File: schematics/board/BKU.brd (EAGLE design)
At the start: 94 x 94 mm, 66 parts, among them Q1 8MHz, Q2 32,768KHz, U1 STM32F405RGT6

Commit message: Добавлена батарейка в БКУ
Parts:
- added BT1: 6.8MM_COIN_CELL, SparkFun-Batteries:BATTCON-6.8MM
- added D1: BB141, diode:SOD523
- added R4: 620R, resistor:R0603
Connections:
- removed net VBAT: U1.1
- new net N$1: BT1.+, R4.1
- new net N$2: D1.C, R4.2, U1.1
- net GND: now also BT1.-
- net VDD: now also D1.A

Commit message: Изменения в БКУ
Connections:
- net 5V: now also RADIO.P$6
- net VDD: no longer RADIO.P$6
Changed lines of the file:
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@@
 <wire x1="0" y1="59.5" x2="0" y2="34.5" width="0.1524" layer="20"/>
 <wire x1="0" y1="23" x2="0" y2="25.5" width="0.1524" layer="20"/>
-<hole x="46.5" y="30" drill="6.5"/>
-<circle x="46.5" y="30" radius="4.5" width="0.1524" layer="21"/>
+<hole x="46" y="30" drill="6.5"/>
+<circle x="46" y="30" radius="4.5" width="0.1524" layer="21"/>
 <rectangle x1="39.972" y1="40.038" x2="51.972" y2="57.038" layer="29" rot="R180"/>
 <rectangle x1="39.97" y1="40.04" x2="51.97" y2="57.04" layer="41"/>
@@
 <wire x1="65.61" y1="32.57" x2="65.33" y2="32.85" width="0.25" layer="1"/>
 <wire x1="65.33" y1="32.85" x2="63.84" y2="32.85" width="0.25" layer="1"/>
+<contactref element="RADIO" pad="P$6"/>
+<wire x1="53.5" y1="76.55" x2="60.97" y2="86.6" width="0" layer="19" extent="1-1"/>
 <wire x1="83.73" y1="64.6" x2="60.97" y2="86.6" width="0" layer="19" extent="1-1"/>
 <wire x1="86.6" y1="53.35" x2="83.73" y2="64.6" width="0" layer="19" extent="1-1"/>
@@
 <contactref element="U$20" pad="10"/>
 <contactref element="U$6" pad="NC/3V3"/>
-<contactref element="RADIO" pad="P$6"/>
 <contactref element="GPS" pad="P$5"/>
 <contactref element="LED1" pad="A"/>
@@
 <wire x1="81.45" y1="73.3" x2="85.35" y2="73.3" width="0" layer="19" extent="1-1"/>
 <wire x1="63.51" y1="86.6" x2="81.45" y2="73.3" width="0" layer="19" extent="1-1"/>
-<wire x1="53.5" y1="76.55" x2="63.51" y2="86.6" width="0" layer="19" extent="1-1"/>
-<wire x1="27.74" y1="55.45" x2="53.5" y2="76.55" width="0" layer="19" extent="1-1"/>
-<wire x1="27.74" y1="48.95" x2="27.74" y2="55.45" width="0" layer="19" extent="1-1"/>
-<wire x1="24.32" y1="46.03" x2="27.74" y2="48.95" width="0" layer="19" extent="1-1"/>
-<wire x1="20.61" y1="40.43" x2="24.32" y2="46.03" width="0" layer="19" extent="1-1"/>
-<wire x1="28.65" y1="39.01" x2="20.61" y2="40.43" width="0" layer="19" extent="1-1"/>
-<wire x1="30.46" y1="38.67" x2="28.65" y2="39.01" width="0" layer="19" extent="1-1"/>
-<wire x1="32.61" y1="38.67" x2="30.46" y2="38.67" width="0" layer="19" extent="1-1"/>
-<wire x1="27.99" y1="33" x2="28.65" y2="39.01" width="0" layer="19" extent="1-1"/>
-<wire x1="16.4" y1="47.95" x2="24.32" y2="46.03" width="0" layer="19" extent="1-1"/>
-<wire x1="13.75" y1="51.4" x2="16.4" y2="47.95" width="0" layer="19" extent="1-1"/>
-<wire x1="12.15" y1="55.6" x2="13.75" y2="51.4" width="0" layer="19" extent="1-1"/>
-<wire x1="12.15" y1="57.75" x2="12.15" y2="55.6" width="0" layer="19" extent="1-1"/>
-<wire x1="18.32" y1="57.37" x2="12.15" y2="57.75" width="0" layer="19" extent="1-1"/>
-<wire x1="7.1" y1="62.75" x2="12.15" y2="57.75" width="0" layer="19" extent="1-1"/>
-<wire x1="7.1" y1="65.25" x2="7.1" y2="62.75" width="0" layer="19" extent="1-1"/>
-<wire x1="15.03" y1="76.28" x2="7.1" y2="65.25" width="0" layer="19" extent="1-1"/>
-<wire x1="7.1" y1="30.75" x2="20.61" y2="40.43" width="0" layer="19" extent="1-1"/>
-<wire x1="42.19" y1="20" x2="27.99" y2="33" width="0" layer="19" extent="1-1"/>
+<wire x1="53.22" y1="36.73" x2="81.45" y2="73.3" width="0" layer="19" extent="1-1"/>
+<wire x1="42.19" y1="20" x2="53.52" y2="32.53" width="0" layer="19" extent="1-1"/>
 <wire x1="46.25" y1="15.2" x2="42.19" y2="20" width="0" layer="19" extent="1-1"/>
 <wire x1="47.65" y1="15.2" x2="46.25" y2="15.2" width="0" layer="19" extent="1-1"/>
@@
 <wire x1="81.35" y1="23" x2="74.65" y2="19.6" width="0" layer="19" extent="1-1"/>
 <wire x1="85.25" y1="23" x2="81.35" y2="23" width="0" layer="19" extent="1-1"/>
-<wire x1="53.52" y1="32.53" x2="42.19" y2="20" width="0" layer="19" extent="1-1"/>
-<wire x1="16.72" y1="11.94" x2="7.1" y2="30.75" width="0" layer="19" extent="1-1"/>
-<wire x1="18.28" y1="9.84" x2="16.72" y2="11.94" width="0" layer="19" extent="1-1"/>
-<wire x1="30" y1="12.2" x2="18.28" y2="9.84" width="0" layer="19" extent="1-1"/>
+<wire x1="30" y1="12.2" x2="42.19" y2="20" width="0" layer="19" extent="1-1"/>
+<wire x1="18.28" y1="9.84" x2="30" y2="12.2" width="0" layer="19" extent="1-1"/>
+<wire x1="16.72" y1="11.94" x2="18.28" y2="9.84" width="0" layer="19" extent="1-1"/>
+<wire x1="27.99" y1="33" x2="42.19" y2="20" width="0" layer="19" extent="1-1"/>
+<wire x1="28.65" y1="39.01" x2="27.99" y2="33" width="0" layer="19" extent="1-1"/>
+<wire x1="30.46" y1="38.67" x2="28.65" y2="39.01" width="0" layer="19" extent="1-1"/>
+<wire x1="32.61" y1="38.67" x2="30.46" y2="38.67" width="0" layer="19" extent="1-1"/>
+<wire x1="20.61" y1="40.43" x2="28.65" y2="39.01" width="0" layer="19" extent="1-1"/>
+<wire x1="24.32" y1="46.03" x2="20.61" y2="40.43" width="0" layer="19" extent="1-1"/>
+<wire x1="27.74" y1="48.95" x2="24.32" y2="46.03" width="0" layer="19" extent="1-1"/>
+<wire x1="27.74" y1="55.45" x2="27.74" y2="48.95" width="0" layer="19" extent="1-1"/>
+<wire x1="16.4" y1="47.95" x2="24.32" y2="46.03" width="0" layer="19" extent="1-1"/>
+<wire x1="13.75" y1="51.4" x2="16.4" y2="47.95" width="0" layer="19" extent="1-1"/>
+<wire x1="12.15" y1="55.6" x2="13.75" y2="51.4" width="0" layer="19" extent="1-1"/>
+<wire x1="12.15" y1="57.75" x2="12.15" y2="55.6" width="0" layer="19" extent="1-1"/>
+<wire x1="18.32" y1="57.37" x2="12.15" y2="57.75" width="0" layer="19" extent="1-1"/>
+<wire x1="7.1" y1="62.75" x2="12.15" y2="57.75" width="0" layer="19" extent="1-1"/>
+<wire x1="7.1" y1="65.25" x2="7.1" y2="62.75" width="0" layer="19" extent="1-1"/>
+<wire x1="15.03" y1="76.28" x2="7.1" y2="65.25" width="0" layer="19" extent="1-1"/>
+<wire x1="7.1" y1="30.75" x2="20.61" y2="40.43" width="0" layer="19" extent="1-1"/>
 </signal>
 <signal name="N$24">

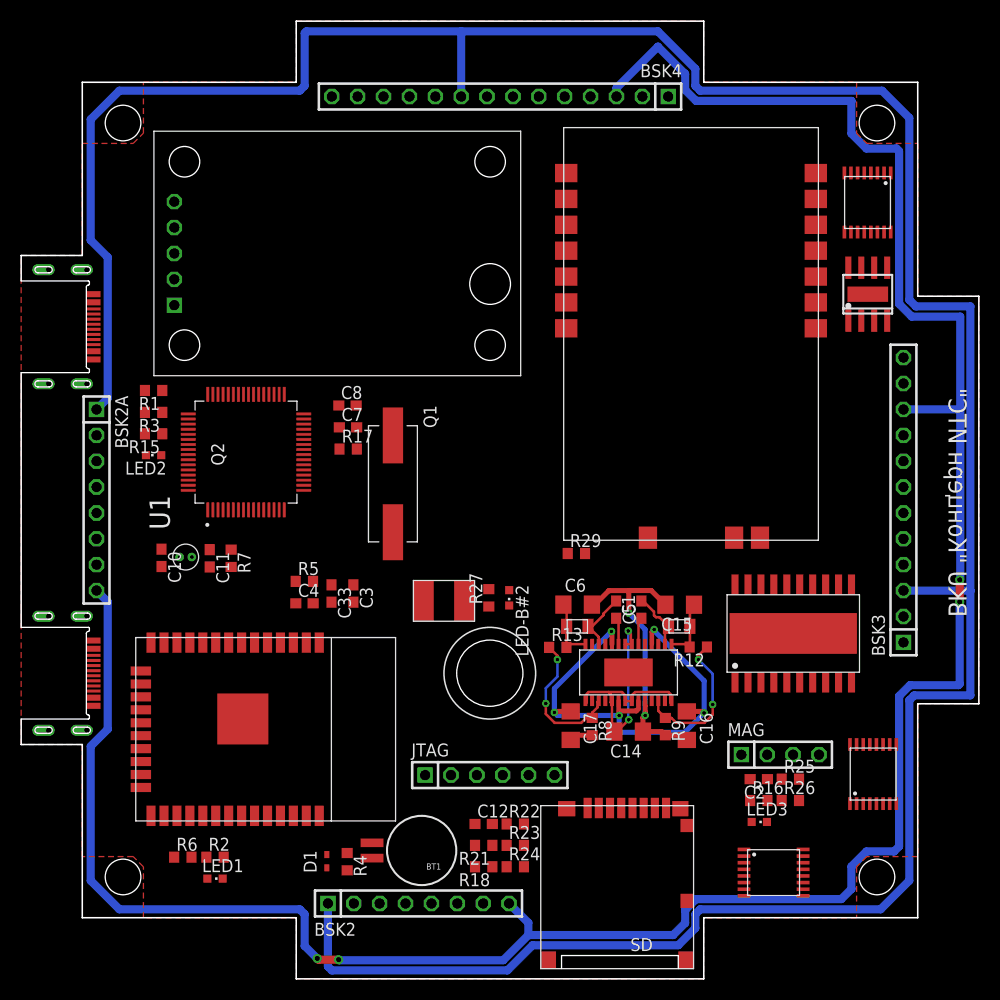
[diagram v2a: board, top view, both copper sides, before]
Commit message: Разводка БКУ кроме 1 дорожки к есп (RX-R)
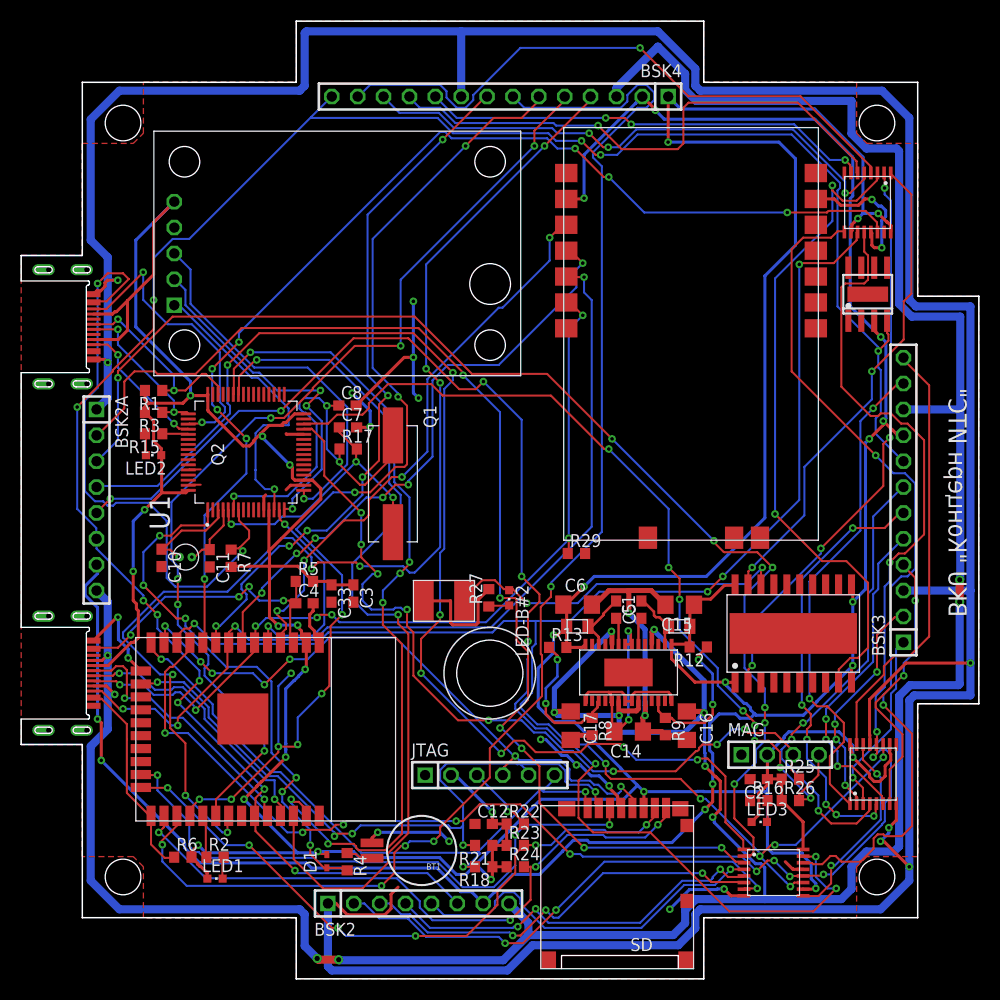
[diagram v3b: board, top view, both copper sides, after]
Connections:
- net TIME-ES: now also U1.15
- net TIME-G: now also U1.14
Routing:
- net VDD: track 6.34 -> 455.7 mm, vias 0 -> 22
- net 5V: track 6.21 -> 237.7 mm, vias 0 -> 12
- net 1W: track 0.00 -> 206.2 mm, vias 0 -> 11
- net STCP: track 0.00 -> 162.8 mm, vias 0 -> 12
- net SHCP: track 0.00 -> 162.1 mm, vias 0 -> 10
- net GND: track 319.5 -> 458.8 mm, vias 2 -> 24
- net SCLTM: track 0.00 -> 135.6 mm, vias 0 -> 5
- net B2A_KVCC: track 0.00 -> 134.8 mm, vias 0 -> 8
- net B2A_KHEAT: track 0.00 -> 120.6 mm, vias 0 -> 7
- net B2A_KEM+: track 0.00 -> 119.5 mm, vias 0 -> 7
- net TIME: track 0.00 -> 116.9 mm, vias 0 -> 8
- net B2A_KEM-: track 0.00 -> 115.0 mm, vias 0 -> 6
- net DS: track 0.00 -> 110.2 mm, vias 0 -> 8
- net SDATM: track 0.00 -> 106.1 mm, vias 0 -> 10
- net I2CINT: track 0.00 -> 96.9 mm, vias 0 -> 6
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
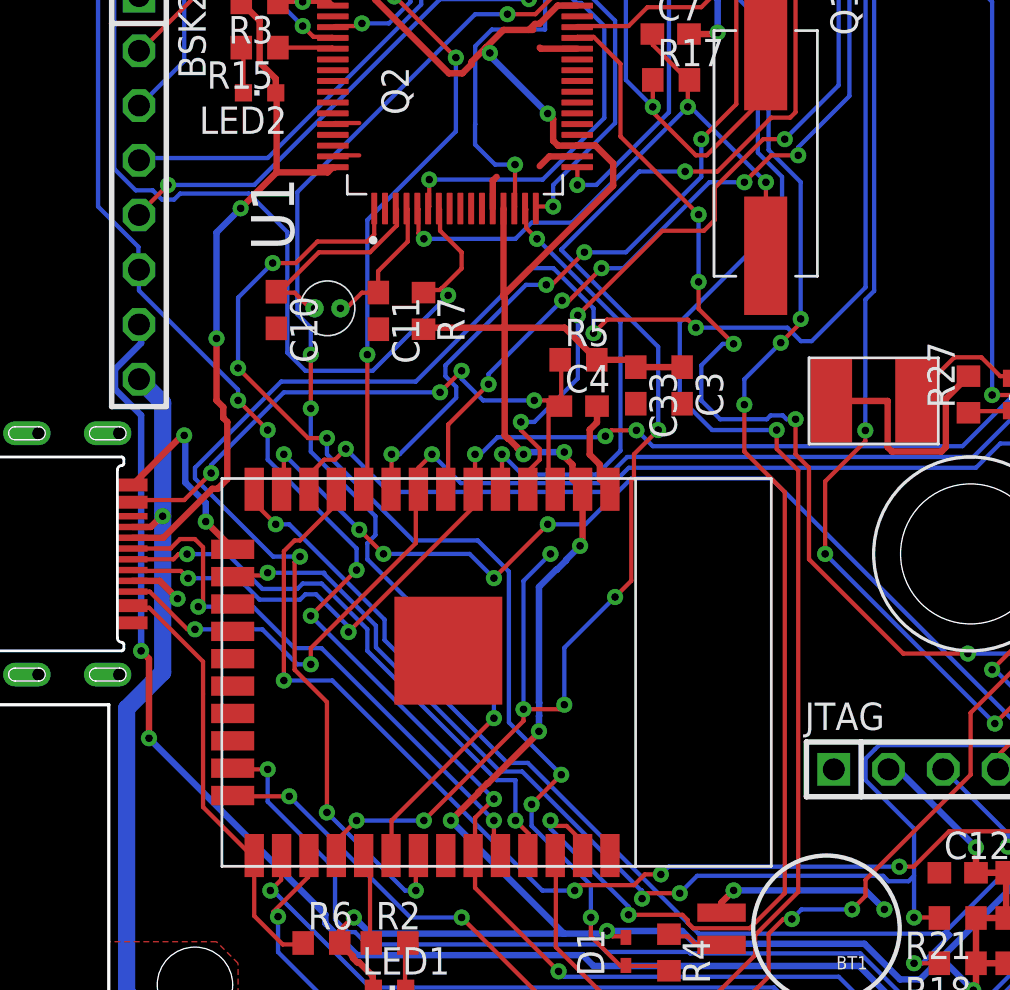
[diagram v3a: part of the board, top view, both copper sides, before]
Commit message: На плате БКУ проведена дорожка RX-R
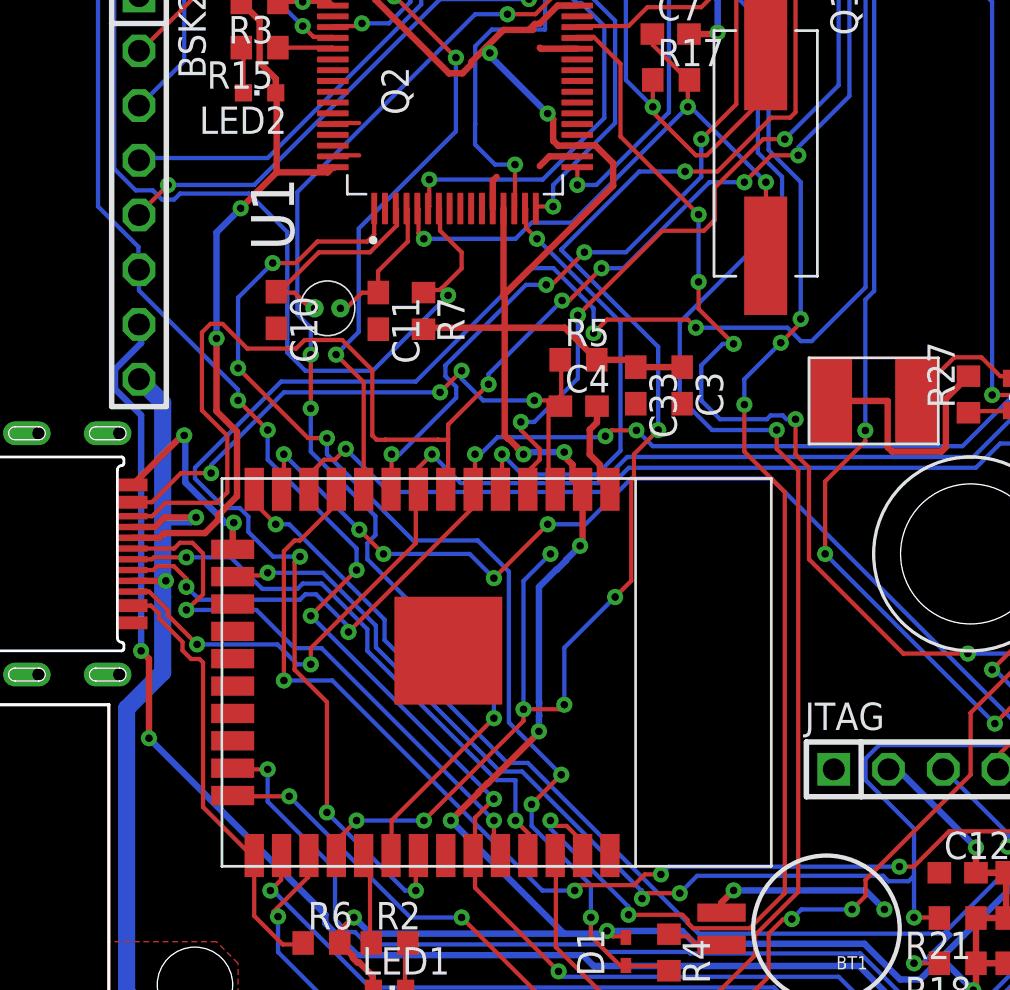
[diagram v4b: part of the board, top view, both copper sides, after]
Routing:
- net RX-R: track 58.8 -> 87.5 mm
- net BUS+: track 322.1 -> 324.5 mm
- net VDD: track 455.7 -> 456.9 mm
- net DS: track 110.2 -> 111.3 mm
- net RX-E: track 26.1 -> 26.7 mm

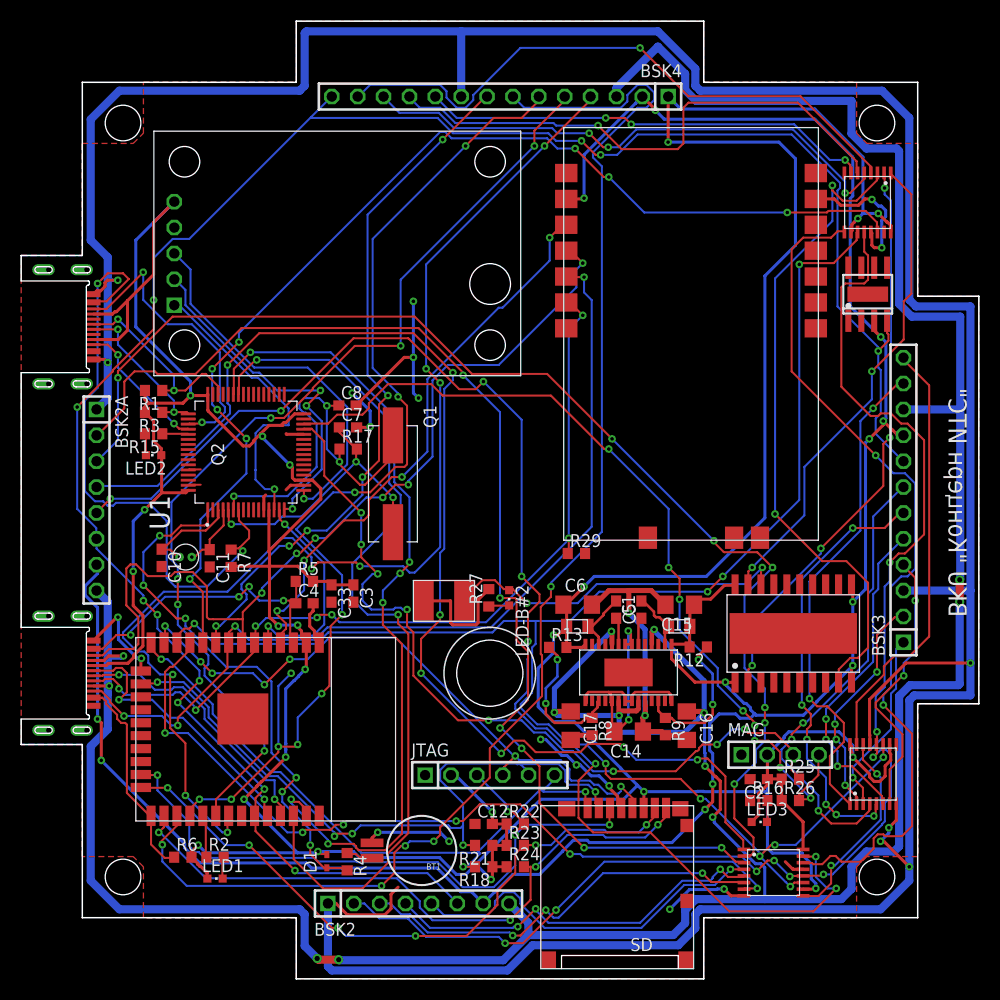
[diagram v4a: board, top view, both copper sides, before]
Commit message: Добавлены подтяжки i2c
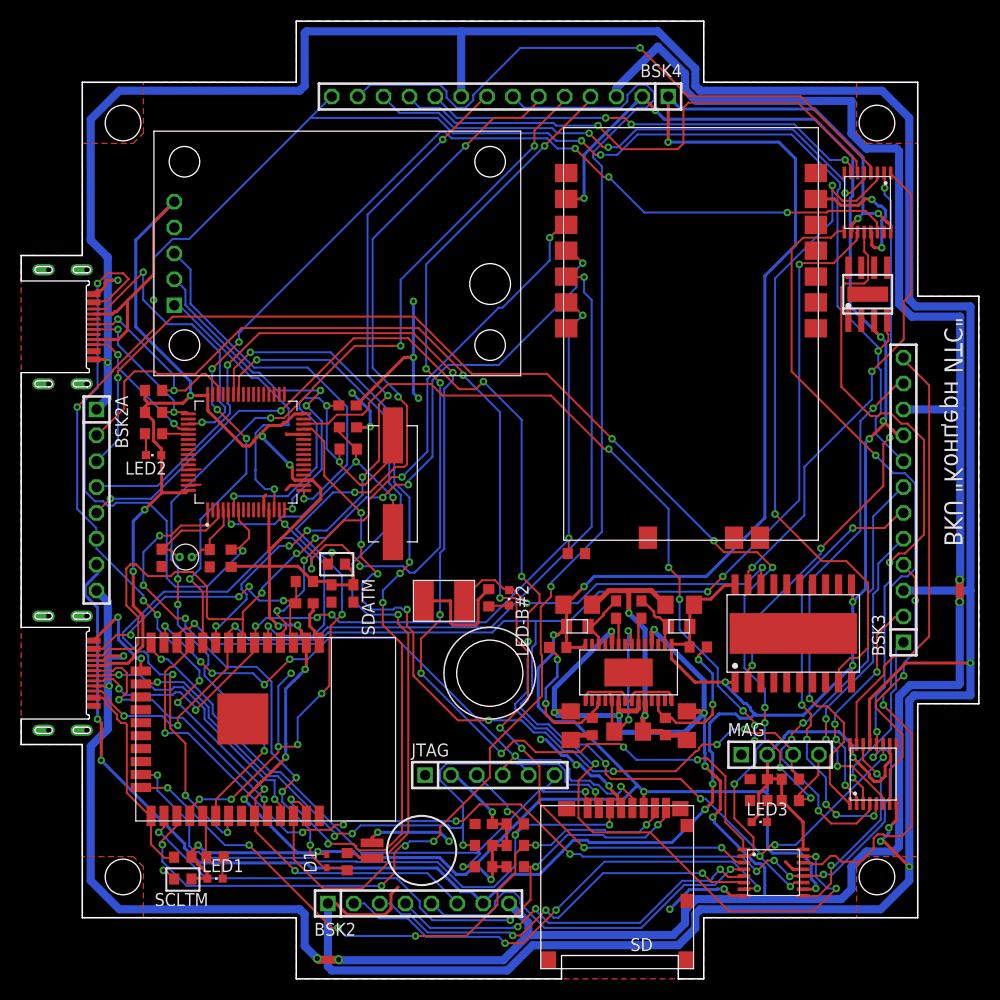
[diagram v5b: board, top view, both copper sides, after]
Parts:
- added R10, R11: 5k1, resistor:R0603
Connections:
- net SCLTM: now also R10.2
- net SDATM: now also R11.2
- net VDD: now also R10.1, R11.1
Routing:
- net SDATM: track 106.1 -> 108.6 mm, vias 10 -> 11
- net TIME: track 117.3 -> 119.5 mm
- net SCLTM: track 135.6 -> 137.6 mm, vias 5 -> 6
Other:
- outline, holes or cut-outs redrawn
- board text added: "SCLTM"
- board text added: "SDATM"
